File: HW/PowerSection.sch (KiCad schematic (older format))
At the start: 33 parts, among them J20 220V~, J21 ph_1x2, J22 s14500, J23 s18650, J24 ph_1x3, J25 ph_1x2, Q20 IRLML2244, U20 IRM-05, U21 MCP73832T-2ACI, U22 BD49K35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

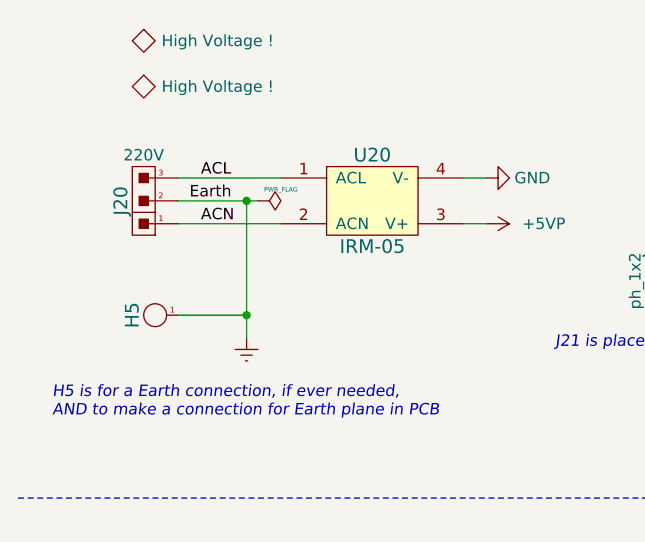
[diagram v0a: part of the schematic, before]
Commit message: Changes the high-voltage section
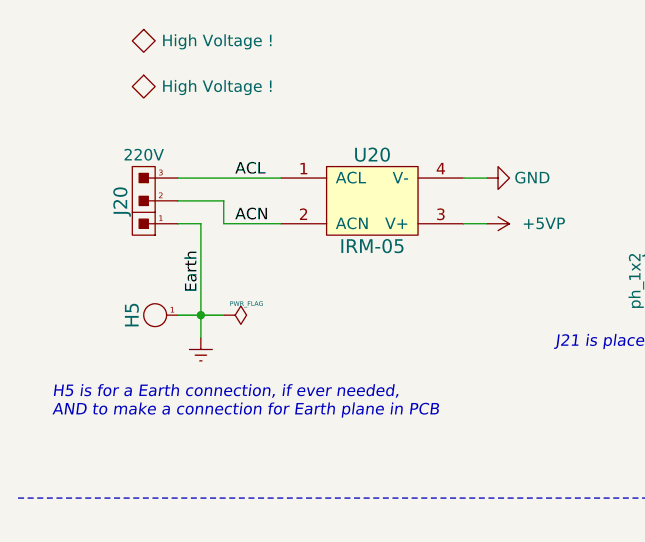
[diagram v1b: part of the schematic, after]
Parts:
- J20: footprint CalinConnectors:SMD_Pins_Big_1x3 -> CalinConnectors:THT_Pins_Big_1x3
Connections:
- wire segments 108 -> 110
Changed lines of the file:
@@
 Sheet 2 3
 Title "ESP32 RFM69/RFM9x Gateway"
-Date "2019-04-21"
-Rev "26"
+Date "2019-04-22"
+Rev "27"
 Comp "Calin Radoni"
 Comment1 ""
@@
 	1    0    0    -1
 $EndComp
-Text Label 1650 1800 0    50   ~ 0
+Text Label 1700 2200 1    50   ~ 0
 Earth
 $Comp
@@
 L power:PWR_FLAG #FLG?
 U 1 1 5CC2CA8F
-P 1950 1800
+P 1800 2300
 AR Path="/5CC2CA8F" Ref="#FLG?"  Part="1"
 AR Path="/5CBFFED5/5CC2CA8F" Ref="#FLG0101"  Part="1"
-F 0 "#FLG0101" H 1950 1875 50  0001 C CNN
-F 1 "PWR_FLAG" V 1900 1900 20  0000 C CNN
-F 2 "" H 1950 1800 50  0001 C CNN
-F 3 "~" H 1950 1800 50  0001 C CNN
-	1    1950 1800
+F 0 "#FLG0101" H 1800 2375 50  0001 C CNN
+F 1 "PWR_FLAG" V 1750 2400 20  0000 C CNN
+F 2 "" H 1800 2300 50  0001 C CNN
+F 3 "~" H 1800 2300 50  0001 C CNN
+	1    1800 2300
 	0    1    1    0
 $EndComp
@@
 L power:Earth #PWR?
 U 1 1 5CC2CAC9
-P 1900 2400
+P 1700 2400
 AR Path="/5CC2CAC9" Ref="#PWR?"  Part="1"
 AR Path="/5CBFFED5/5CC2CAC9" Ref="#PWR0112"  Part="1"
-F 0 "#PWR0112" H 1900 2150 50  0001 C CNN
-F 1 "Earth" H 1900 2250 50  0001 C CNN
-F 2 "" H 1900 2400 50  0001 C CNN
-F 3 "~" H 1900 2400 50  0001 C CNN
-	1    1900 2400
-	1    0    0    -1
-$EndComp
-Text Label 1700 1900 0    50   ~ 0
+F 0 "#PWR0112" H 1700 2150 50  0001 C CNN
+F 1 "Earth" H 1700 2250 50  0001 C CNN
+F 2 "" H 1700 2400 50  0001 C CNN
+F 3 "~" H 1700 2400 50  0001 C CNN
+	1    1700 2400
+	1    0    0    -1
+$EndComp
+Text Label 1850 1900 0    50   ~ 0
 ACN
-Text Label 1700 1700 0    50   ~ 0
+Text Label 1850 1700 0    50   ~ 0
 ACL
-Wire Wire Line
-	1600 1900 2050 1900
 Wire Wire Line
 	1600 1700 2050 1700
@@
 F 0 "J20" V 1550 1800 60  0000 C CNN
 F 1 "220V~" H 1450 1600 50  0000 C CNN
-F 2 "CalinConnectors:SMD_Pins_Big_1x3" H 1450 1900 60  0001 C CNN
+F 2 "CalinConnectors:THT_Pins_Big_1x3" H 1450 1900 60  0001 C CNN
 F 3 "" H 1450 1900 60  0000 C CNN
 	1    1450 1800
@@
 ChargeStatus
 Wire Wire Line
-	1600 1800 1900 1800
-Wire Wire Line
-	1900 1800 1900 2300
-Wire Wire Line
-	1600 2300 1900 2300
-Connection ~ 1900 2300
-Wire Wire Line
-	1900 2300 1900 2400
-Wire Wire Line
-	1950 1800 1900 1800
-Connection ~ 1900 1800
+	1600 2300 1700 2300
 Wire Notes Line width 20 style dotted
 	5000 3100 900  3100
@@
 Text Notes 1050 2750 0    50   Italic 0
 H5 is for a Earth connection, if ever needed,\nAND to make a connection for Earth plane in PCB
+Wire Wire Line
+	1600 1900 1700 1900
+Wire Wire Line
+	1700 1900 1700 2300
+Wire Wire Line
+	1600 1800 1800 1800
+Wire Wire Line
+	1800 1800 1800 1900
+Wire Wire Line
+	1800 1900 2050 1900
+Wire Wire Line
+	1800 2300 1700 2300
+Connection ~ 1700 2300
+Wire Wire Line
+	1700 2400 1700 2300
 $EndSCHEMATC

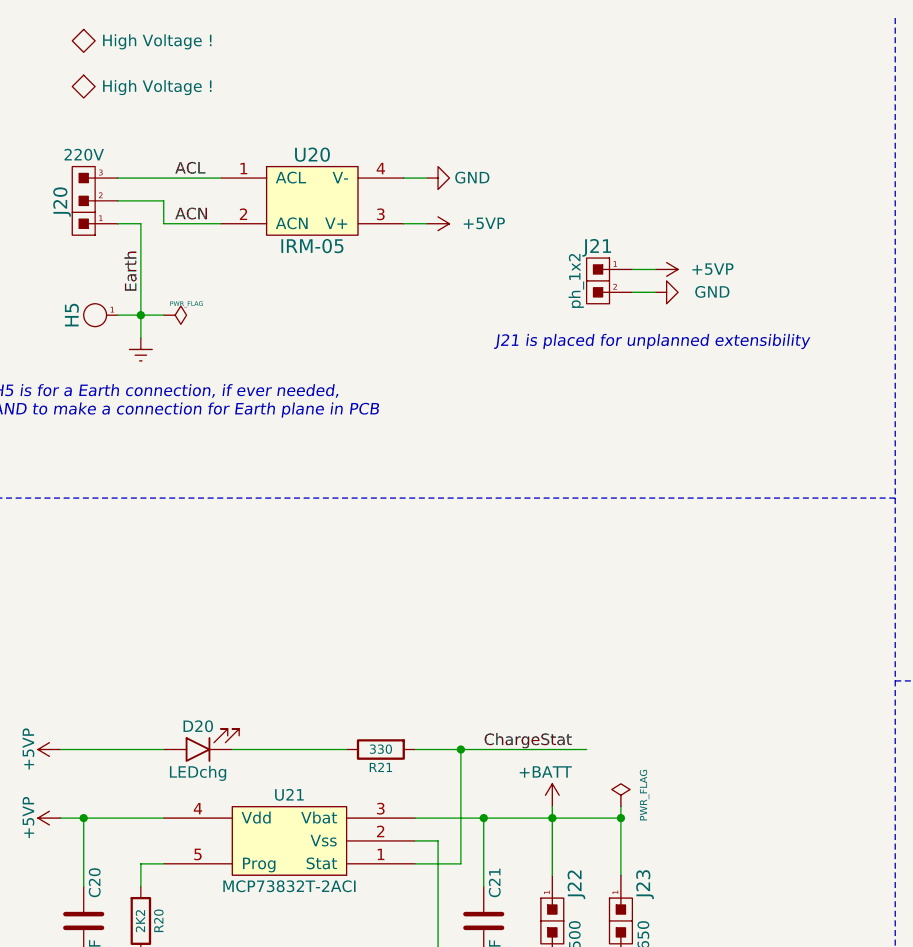
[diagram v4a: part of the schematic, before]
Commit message: Adds a new I2C connector, a LED for 5V indication, some SMD connections for a few free pins and labels
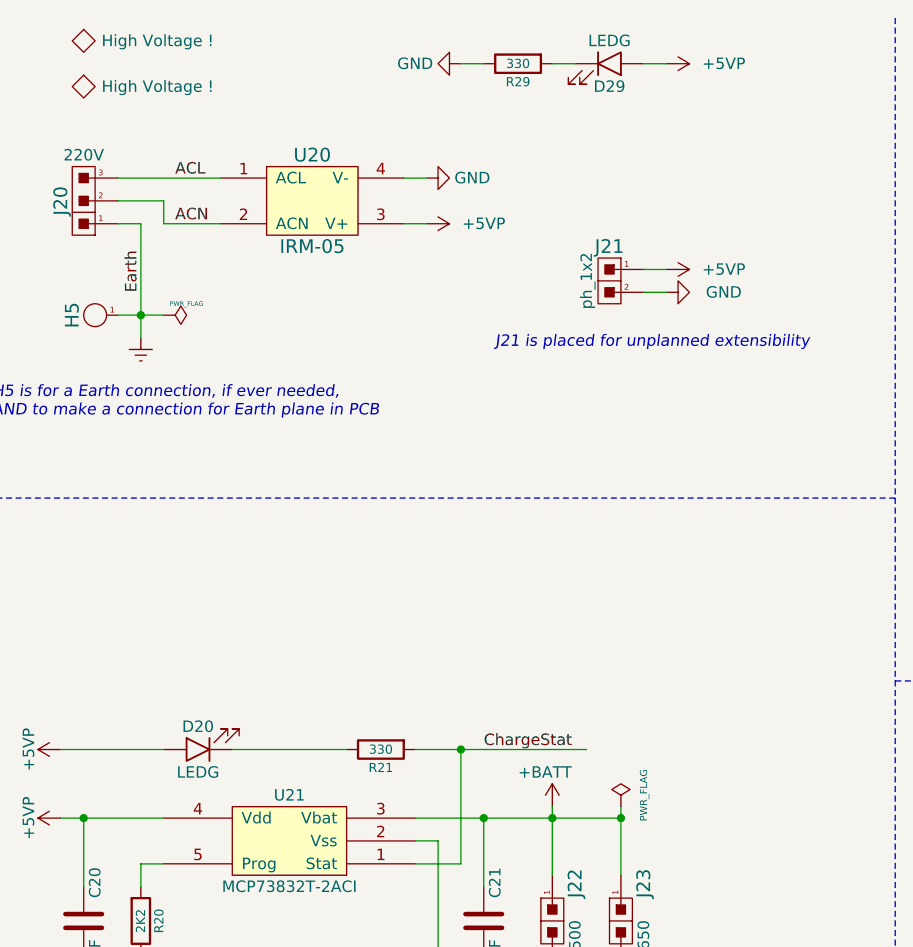
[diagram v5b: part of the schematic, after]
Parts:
- added D29: LEDG, CalinGeneric:LED0805HS, symbol calin:LED
- added R29: 330, CalinGeneric:R0805HS, symbol calin:R
- D20: value LEDchg -> LEDG
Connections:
- wire segments 110 -> 113
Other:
- moved on the sheet: J21
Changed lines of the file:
@@
 Sheet 2 3
 Title "ESP32 RFM69/RFM9x Gateway"
-Date "2019-04-22"
-Rev "30"
+Date "2019-04-25"
+Rev "32"
 Comp "Calin Radoni"
 Comment1 ""
@@
 $EndComp
 Wire Wire Line
-	3850 2200 3950 2200
-Wire Wire Line
-	3950 2100 3850 2100
+	3900 2200 4000 2200
+Wire Wire Line
+	4000 2100 3900 2100
 $Comp
 L power:GND #PWR?
 U 1 1 5CC2CB07
-P 3950 2200
+P 4000 2200
 AR Path="/5CC2CB07" Ref="#PWR?"  Part="1"
 AR Path="/5CBFFED5/5CC2CB07" Ref="#PWR0114"  Part="1"
-F 0 "#PWR0114" H 3950 1950 50  0001 C CNN
-F 1 "GND" V 3950 1950 50  0000 C CNN
-F 2 "" H 3950 2200 50  0000 C CNN
-F 3 "" H 3950 2200 50  0000 C CNN
-	1    3950 2200
+F 0 "#PWR0114" H 4000 1950 50  0001 C CNN
+F 1 "GND" V 4000 1950 50  0000 C CNN
+F 2 "" H 4000 2200 50  0000 C CNN
+F 3 "" H 4000 2200 50  0000 C CNN
+	1    4000 2200
 	0    -1   -1   0
 $EndComp
@@
 L power:+5VP #PWR?
 U 1 1 5CC2CB0D
-P 3950 2100
+P 4000 2100
 AR Path="/5CC2CB0D" Ref="#PWR?"  Part="1"
 AR Path="/5CBFFED5/5CC2CB0D" Ref="#PWR0123"  Part="1"
-F 0 "#PWR0123" H 3950 1950 50  0001 C CNN
-F 1 "+5VP" V 3950 2350 50  0000 C CNN
-F 2 "" H 3950 2100 50  0000 C CNN
-F 3 "" H 3950 2100 50  0000 C CNN
-	1    3950 2100
+F 0 "#PWR0123" H 4000 1950 50  0001 C CNN
+F 1 "+5VP" V 4000 2350 50  0000 C CNN
+F 2 "" H 4000 2100 50  0000 C CNN
+F 3 "" H 4000 2100 50  0000 C CNN
+	1    4000 2100
 	0    1    1    0
 $EndComp
@@
 L calin:CS_2s J?
 U 1 1 5CC2CB13
-P 3700 2150
+P 3750 2150
 AR Path="/5CC2CB13" Ref="J?"  Part="1"
 AR Path="/5CBFFED5/5CC2CB13" Ref="J21"  Part="1"
-F 0 "J21" H 3700 2300 60  0000 C CNN
-F 1 "ph_1x2" V 3800 2150 50  0000 C CNN
-F 2 "CalinConnectors:Pin_Header_Straight_1x02" H 3700 2200 60  0001 C CNN
-F 3 "" H 3700 2200 60  0000 C CNN
-	1    3700 2150
+F 0 "J21" H 3750 2300 60  0000 C CNN
+F 1 "ph_1x2" V 3850 2150 50  0000 C CNN
+F 2 "CalinConnectors:Pin_Header_Straight_1x02" H 3750 2200 60  0001 C CNN
+F 3 "" H 3750 2200 60  0000 C CNN
+	1    3750 2150
 	-1   0    0    -1
 $EndComp
@@
 AR Path="/5CBFFED5/5CC2CB8D" Ref="D20"  Part="1"
 F 0 "D20" H 1950 4100 50  0000 C CNN
-F 1 "LEDchg" H 1950 4300 50  0000 C CNN
+F 1 "LEDG" H 1950 4300 50  0000 C CNN
 F 2 "CalinGeneric:LED0805HS" H 1950 4200 50  0001 C CNN
 F 3 "" H 1950 4200 50  0001 C CNN
@@
 Wire Wire Line
 	1700 2400 1700 2300
+$Comp
+L calin:R R?
+U 1 1 5CC2393E
+P 3350 1200
+AR Path="/5CC2393E" Ref="R?"  Part="1"
+AR Path="/5CBFFED5/5CC2393E" Ref="R29"  Part="1"
+F 0 "R29" V 3430 1200 40  0000 C CNN
+F 1 "330" V 3350 1200 40  0000 C CNN
+F 2 "CalinGeneric:R0805HS" V 3280 1200 30  0001 C CNN
+F 3 "" H 3350 1200 30  0000 C CNN
+	1    3350 1200
+	0    1    1    0
+$EndComp
+$Comp
+L calin:LED D?
+U 1 1 5CC23A10
+P 3750 1200
+AR Path="/5CC23A10" Ref="D?"  Part="1"
+AR Path="/5CBFFED5/5CC23A10" Ref="D29"  Part="1"
+F 0 "D29" H 3750 1100 50  0000 C CNN
+F 1 "LEDG" H 3750 1300 50  0000 C CNN
+F 2 "CalinGeneric:LED0805HS" H 3750 1200 50  0001 C CNN
+F 3 "" H 3750 1200 50  0001 C CNN
+	1    3750 1200
+	1    0    0    -1
+$EndComp
+$Comp
+L power:GND #PWR?
+U 1 1 5CC23BE5
+P 3100 1200
+AR Path="/5CC23BE5" Ref="#PWR?"  Part="1"
+AR Path="/5CBFFED5/5CC23BE5" Ref="#PWR0181"  Part="1"
+F 0 "#PWR0181" H 3100 950 50  0001 C CNN
+F 1 "GND" V 3100 1000 50  0000 C CNN
+F 2 "" H 3100 1200 50  0000 C CNN
+F 3 "" H 3100 1200 50  0000 C CNN
+	1    3100 1200
+	0    1    1    0
+$EndComp
+$Comp
+L power:+5VP #PWR?
+U 1 1 5CC23D54
+P 4000 1200
+AR Path="/5CC23D54" Ref="#PWR?"  Part="1"
+AR Path="/5CBFFED5/5CC23D54" Ref="#PWR0182"  Part="1"
+F 0 "#PWR0182" H 4000 1050 50  0001 C CNN
+F 1 "+5VP" V 4000 1450 50  0000 C CNN
+F 2 "" H 4000 1200 50  0000 C CNN
+F 3 "" H 4000 1200 50  0000 C CNN
+	1    4000 1200
+	0    1    1    0
+$EndComp
+Wire Wire Line
+	4000 1200 3900 1200
+Wire Wire Line
+	3600 1200 3500 1200
+Wire Wire Line
+	3200 1200 3100 1200
 $EndSCHEMATC

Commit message: Updates components to add manufacturer, part number, ... fields. Also checked some values.
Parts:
- C20, C21: symbol Device:C -> calin:C; characteristics (none) -> 10 µF / 6,3 V; manufacturer (none) -> Samsung; package (none) -> 0805; part-number (none) -> CL21B106KQQNNNE
- C22, C26: symbol Device:C -> calin:C; characteristics (none) -> 100 nF / 50V / X7R; manufacturer (none) -> Samsung; package (none) -> 0805; part-number (none) -> CL21B104KBCNNNC
- C23: value 10uF -> 10uF/10V/1mOhm; symbol Device:C -> calin:C; characteristics (none) -> 10 µF / 16 V / X7R / ESR: 1 mΩ; manufacturer (none) -> Taiyo Yuden; package (none) -> 0805; part-number (none) -> EMK212BB7106KG-T
- C24: value 22uF/1mOhm -> 22uF/6.3V/1mOhm; symbol Device:C -> calin:C; characteristics (none) -> 22 µF / 6.3 V / X5R / ESR: 1 mΩ; manufacturer (none) -> Taiyo Yuden; package (none) -> 0805; part-number (none) -> JMK212BJ226MG-T
- C25: symbol Device:C -> calin:C; characteristics (none) -> 100pF / 50V / X7R; manufacturer (none) -> Wurth Electronics; package (none) -> 0805; part-number (none) -> 885012207080
- D20: value LEDG -> LED-DNP; Notes (none) -> DNP; Variant (none) -> DNP; part-number (none) -> DNP
- D21: characteristics (none) -> 3A schottky rectifier; manufacturer (none) -> Diodes; package (none) -> SMA; part-number (none) -> B340AE-13
- D29: value LEDG -> LED Green; Variant (none) -> test
- H5, J20: Notes (none) -> DNP; Variant (none) -> pcb
- J21: Notes (none) -> DNP; Variant (none) -> test
- J22: Variant (none) -> 14500
- J23: Variant (none) -> 18650
- J24, J25: Variant (none) -> test
- L21: manufacturer (none) -> Abracon Corporation; part-number (none) -> ASPI-0530HI-2R2M-T2
- Q20: characteristics (none) -> *; manufacturer (none) -> International Rectifier; package (none) -> SOT23-3; part-number (none) -> IRLML2244TRPbF
- R20: value 2K2 -> 2k2; characteristics (none) -> 2k; manufacturer (none) -> Panasonic; package (none) -> 0805; part-number (none) -> ERJ6ENF2001V
- R21: value 330 -> 330-DNP; Notes (none) -> DNP; characteristics (none) -> 330; manufacturer (none) -> Vishay; package (none) -> 0805; part-number (none) -> DNP
- R22, R23: Source (none) -> Mouser; characteristics (none) -> 2M 1%; manufacturer (none) -> Panasonic; package (none) -> 0805; part-number (none) -> ERJ-6ENF2004V
- R25, R26: characteristics (none) -> 10k; manufacturer (none) -> Vishay; package (none) -> 0805; part-number (none) -> CRCW080510K0FKEA
- R27: Source (none) -> Mouser; characteristics (none) -> 442k 1%; manufacturer (none) -> Panasonic; package (none) -> 0805; part-number (none) -> ERJ-6ENF4423V
- R28: Source (none) -> Mouser; characteristics (none) -> 100k 1%; manufacturer (none) -> Panasonic; package (none) -> 0805; part-number (none) -> ERJ-6ENF1003V
- R29: characteristics (none) -> 330; manufacturer (none) -> Vishay; package (none) -> 0805; part-number (none) -> CRCW0805330RFKTABC
- SYM3, SYM4: Notes (none) -> DNP; Variant (none) -> pcb; part-number (none) -> DNP
- U20: characteristics (none) -> 5W AC-DC module-type power supply; manufacturer (none) -> Mean Well; package (none) -> 222A; part-number (none) -> IRM-05
- U21: symbol calin:MCP73831 -> calin:MCP73832; characteristics (none) -> Single-Cell, Li-Ion, Li-Polymer Charge Management Controlle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; manufacturer (none) -> Microchip; package (none) -> SOT23-5; part-number (none) -> MCP73832T-2ACI
- U22: characteristics (none) -> Standard CMOS Voltage Detector IC 3.5V; manufacturer (none) -> ROHM Semiconductor; package (none) -> SSOP3 (SOT23-3); part-number (none) -> BD49K35
- U23: characteristics (none) -> Step-Down Converter 2A 1.5MHz Iq=35uA; manufacturer (none) -> Texas Instrumnets; package (none) -> SOT23-5; part-number (none) -> TLV62569DBV
- U24: characteristics (none) -> MicroPower 4 μA, Low Offset Voltage, Unity-Gain Stable, Rai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; manufacturer (none) -> Texas Instruments; package (none) -> SOT23-5; part-number (none) -> TLV379IDBV

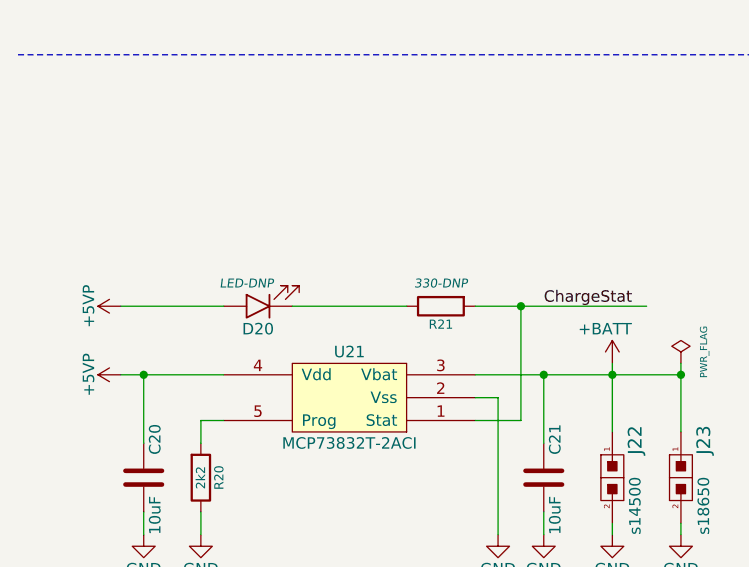
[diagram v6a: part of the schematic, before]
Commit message: Changes C4 to NC to prevent unwanted boot to Download mode and removes keepout area from under the ESP32 module.
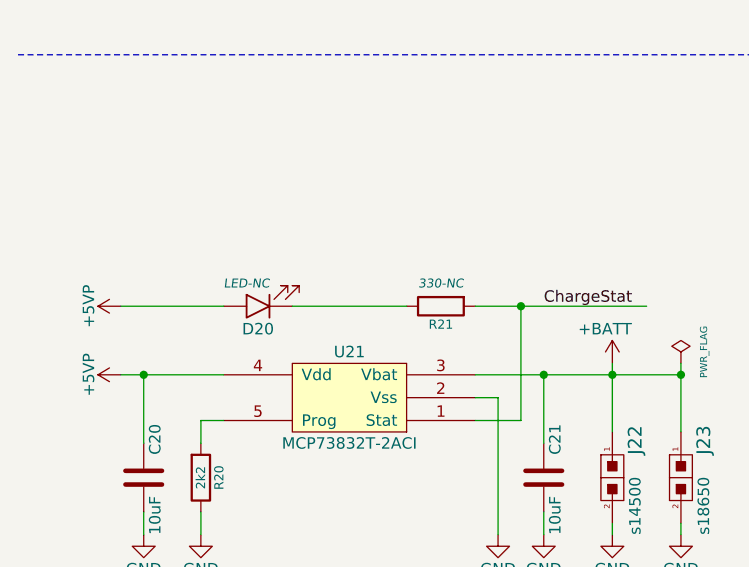
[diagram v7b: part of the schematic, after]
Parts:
- D20: value LED-DNP -> LED-NC
- R21: value 330-DNP -> 330-NC
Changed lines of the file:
@@
 Title "ESP32 RFM69/RFM9x Gateway"
 Date "2019-05-02"
-Rev "33"
+Rev "34"
 Comp "Calin Radoni"
 Comment1 ""
@@
 AR Path="/5CBFFED5/5CC2CB8D" Ref="D20"  Part="1"
 F 0 "D20" H 1950 4300 50  0000 C CNN
-F 1 "LED-DNP" H 2000 4100 39  0000 C CIN
+F 1 "LED-NC" H 2000 4100 39  0000 C CIN
 F 2 "CalinGeneric:LED0805HS" H 1950 4200 50  0001 C CNN
 F 3 "" H 1950 4200 50  0001 C CNN
@@
 AR Path="/5CBFFED5/5CC2CBB7" Ref="R21"  Part="1"
 F 0 "R21" V 2830 4200 40  0000 C CNN
-F 1 "330-DNP" V 2650 4200 39  0000 C CIN
+F 1 "330-NC" V 2650 4200 39  0000 C CIN
 F 2 "CalinGeneric:R0805HS" V 2680 4200 30  0001 C CNN
 F 3 "" H 2750 4200 30  0000 C CNN
